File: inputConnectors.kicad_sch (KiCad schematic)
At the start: 2 parts

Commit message: Changes to final schematic
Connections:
- net ESP_USB_DM renamed ESP_USB_D-
- net ESP_USB_DP renamed ESP_USB_D+
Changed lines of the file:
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@@
 		)
 	)
-	(label "ESP_USB_DM"
+	(label "ESP_USB_D-"
 		(at 83.82 59.69 0)
 		(effects
@@
 		)
 	)
-	(label "ESP_USB_DM"
+	(label "ESP_USB_D-"
 		(at 27.94 59.69 0)
 		(effects
@@
 		)
 	)
-	(label "ESP_USB_DP"
+	(label "ESP_USB_D+"
 		(at 27.94 57.15 0)
 		(effects
@@
 		)
 	)
-	(label "ESP_USB_DP"
+	(label "ESP_USB_D+"
 		(at 83.82 57.15 0)
 		(effects
@@
 		)
 	)
-	(global_label "ESP_USB_DP"
+	(global_label "ESP_USB_D+"
 		(shape output)
 		(at 96.52 57.15 0)
@@
 		)
 		(property "Intersheetrefs" "${INTERSHEET_REFS}"
-			(at 108.2513 57.15 0)
+			(at 108.4894 57.15 0)
 			(effects
 				(font
@@
 		)
 	)
-	(global_label "ESP_USB_DM"
+	(global_label "ESP_USB_D-"
 		(shape output)
 		(at 96.52 59.69 0)
@@
 		)
 		(property "Intersheetrefs" "${INTERSHEET_REFS}"
-			(at 108.3942 59.69 0)
+			(at 108.4894 59.69 0)
 			(effects
 				(font

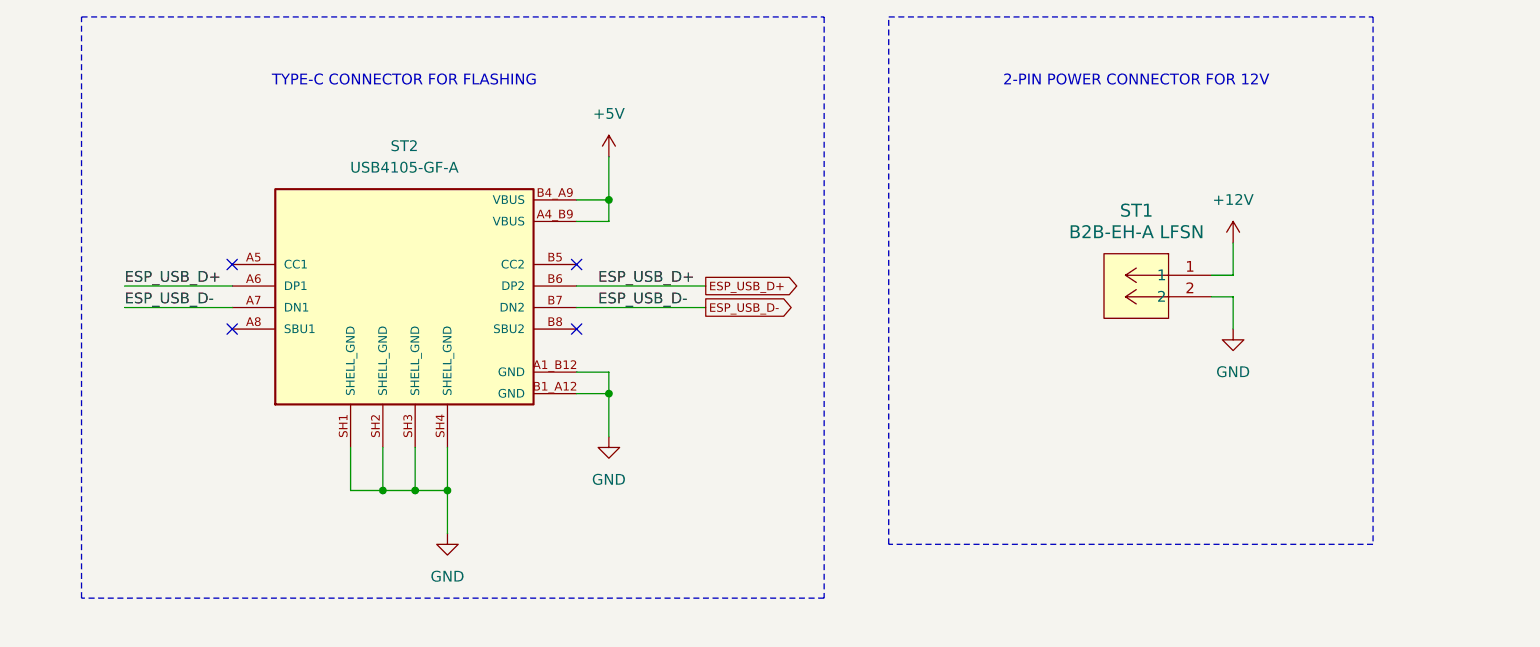
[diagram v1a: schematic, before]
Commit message: Arranged Headers + Added pull-down resistors for type-c conn
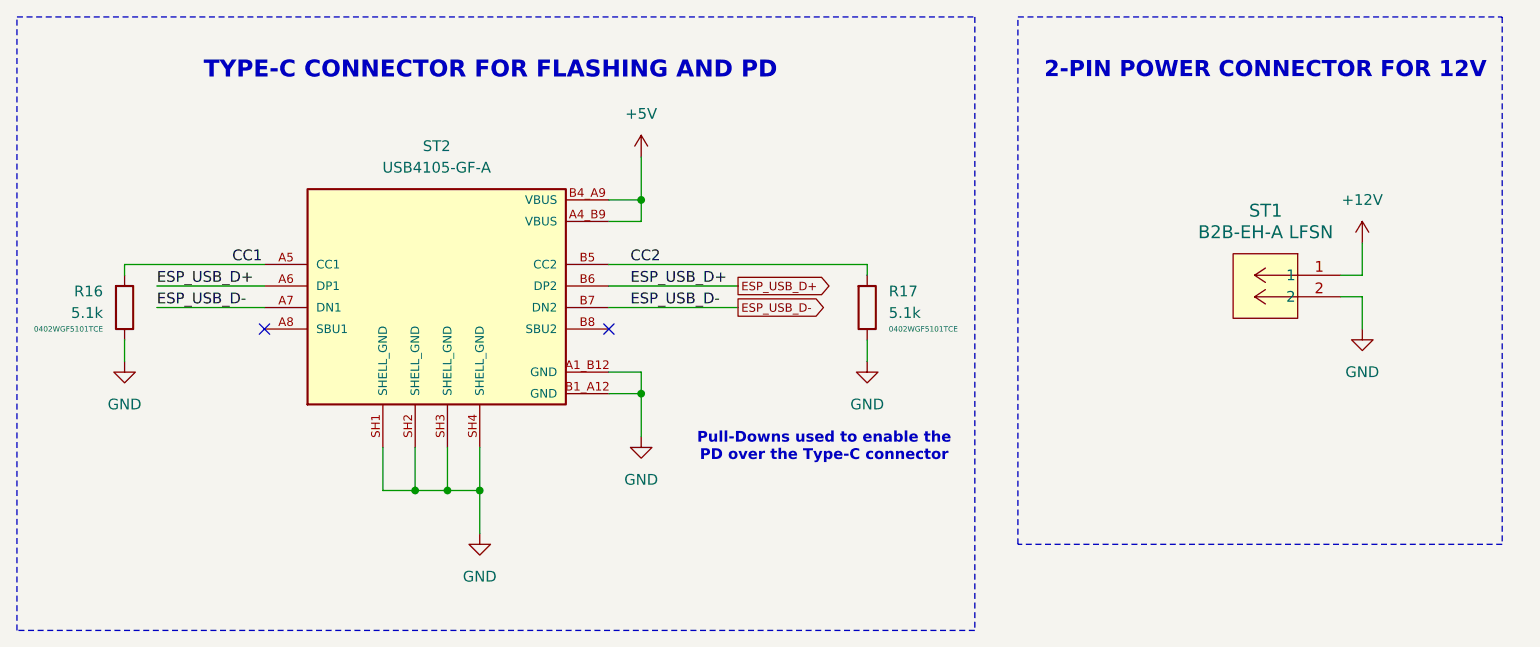
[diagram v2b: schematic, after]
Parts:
- added R16, R17: 5.1k, 0402WGF5101TCE:RESC1005X40N, symbol Project_Resistors:0402WGF5101TCE
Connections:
- net GND: now also R16.2, R17.2
- net CC1: now reaches ST2.A5 (CC1)
- net CC1: now also R16.1
- net CC2: now reaches ST2.B5 (CC2)
- net CC2: now also R17.1
- no-connect marks 4 -> 2
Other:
- note added: "Pull-Downs used to enable the PD over the Type-C connector"
- note added: "TYPE-C CONNECTOR FOR FLASHING AND PD"
- note removed: "TYPE-C CONNECTOR FOR FLASHING"
- moved on the sheet: ST1, ST2

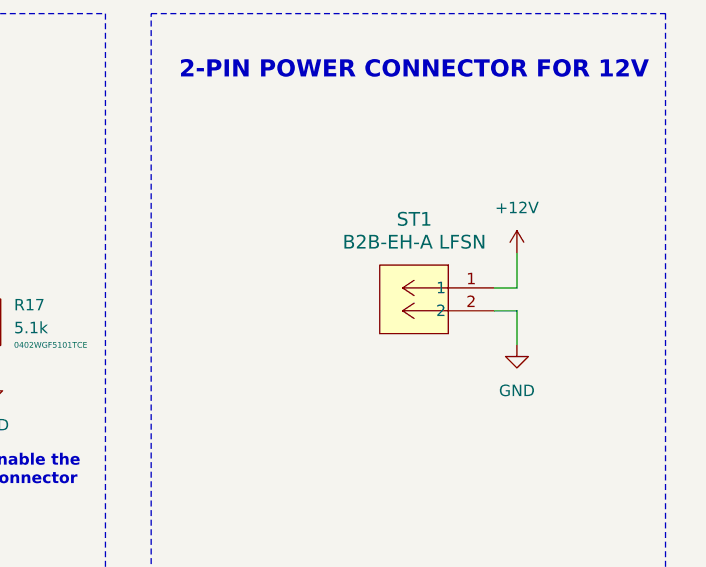
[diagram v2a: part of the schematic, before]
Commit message: JST 2 PIN CONN Changed + Additional 3D Models added
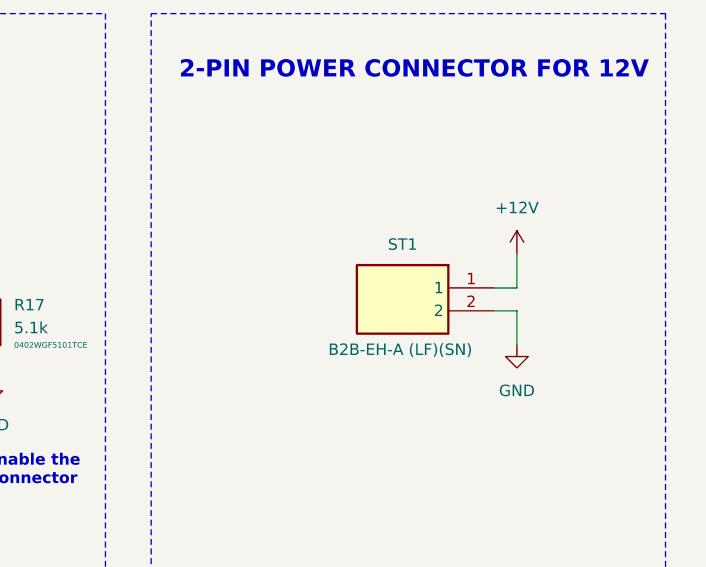
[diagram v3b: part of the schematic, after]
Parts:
- removed ST1: B2B-EH-A LFSN, JST_B2B-EH-A-LF-SN:CONN_B2B-EH-A LFSN_JST, symbol JST_B2B-EH-A-LF-SN:B2B-EH-A_LFSN
- added ST1: B2B-EH-A (LF)(SN), JST_B2B-EH-A(LF)(SN):SHDR2W64P0X250_1X2_750X380X600P, symbol B2B-EH-A(LF)(SN):B2B-EH-A (LF)(SN)
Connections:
- net +12V: now also ST1.1
- net GND: now also ST1.2
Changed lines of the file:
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@@
+	)
+	(symbol
+		(lib_id "B2B-EH-A(LF)(SN):B2B-EH-A (LF)(SN)")
+		(at 171.45 55.88 0)
+		(mirror y)
+		(unit 1)
+		(exclude_from_sim no)
+		(in_bom yes)
+		(on_board yes)
+		(dnp no)
+		(property "Reference" "ST1"
+			(at 161.29 51.054 0)
+			(effects
+				(font
+					(size 1.27 1.27)
+				)
+			)
+		)
+		(property "Value" "B2B-EH-A (LF)(SN)"
+			(at 161.036 62.738 0)
+			(effects
+				(font
+					(size 1.27 1.27)
+				)
+			)
+		)
+		(property "Footprint" "JST_B2B-EH-A(LF)(SN):SHDR2W64P0X250_1X2_750X380X600P"
+			(at 154.94 150.8 0)
+			(effects
+				(font
+					(size 1.27 1.27)
+				)
+				(justify left top)
+				(hide yes)
+			)
+		)
+		(property "Datasheet" "http://www.farnell.com/datasheets/2057210.pdf"
+			(at 154.94 250.8 0)
+			(effects
+				(font
+					(size 1.27 1.27)
+				)
+				(justify left top)
+				(hide yes)
+			)
+		)
+		(property "Description" "JST (JAPAN SOLDERLESS TERMINALS) - B2B-EH-A(LF)(SN) - CONNECTOR, HEADER, 2POS, 2.5MM, 1ROW"
+			(at 171.45 55.88 0)
+			(effects
+				(font
+					(size 1.27 1.27)
+				)
+				(hide yes)
+			)
+		)
+		(property "Height" "6"
+			(at 154.94 450.8 0)
+			(effects
+				(font
+					(size 1.27 1.27)
+				)
+				(justify left top)
+				(hide yes)
+			)
+		)
+		(property "Manufacturer_Name" "JST (JAPAN SOLDERLESS TERMINALS)"
+			(at 154.94 550.8 0)
+			(effects
+				(font
+					(size 1.27 1.27)
+				)
+				(justify left top)
+				(hide yes)
+			)
+		)
+		(property "Manufacturer_Part_Number" "B2B-EH-A(LF)(SN)"
+			(at 154.94 650.8 0)
+			(effects
+				(font
+					(size 1.27 1.27)
+				)
+				(justify left top)
+				(hide yes)
+			)
+		)
+		(property "Mouser Part Number" "N/A"
+			(at 154.94 750.8 0)
+			(effects
+				(font
+					(size 1.27 1.27)
+				)
+				(justify left top)
+				(hide yes)
+			)
+		)
+		(property "Mouser Price/Stock" "https://www.mouser.co.uk/ProductDetail/JST-Commercial/B2B-EH-ALFSN?qs=IKkN%2F947nfCWfpMyWlAobg%3D%3D"
+			(at 154.94 850.8 0)
+			(effects
+				(font
+					(size 1.27 1.27)
+				)
+				(justify left top)
+				(hide yes)
+			)
+		)
+		(property "Arrow Part Number" "B2B-EH-A(LF)(SN)"
+			(at 154.94 950.8 0)
+			(effects
+				(font
+					(size 1.27 1.27)
+				)
+				(justify left top)
+				(hide yes)
+			)
+		)
+		(property "Arrow Price/Stock" "https://www.arrow.com/en/products/b2b-eh-a-lf-sn/jst-manufacturing?region=europe"
+			(at 154.94 1050.8 0)
+			(effects
+				(font
+					(size 1.27 1.27)
+				)
+				(justify left top)
+				(hide yes)
+			)
+		)
+		(pin "2"
+		)
+		(pin "1"
+		)
+		(instances
+			(project ""
+				(path "/fb473f03-1ffd-4345-8dd1-2894c6aef0cc/473821bc-4394-4ccd-b399-e5ac546e238c"
+					(reference "ST1")
+					(unit 1)
+				)
+			)
+		)
 	)
 	(symbol
@@
 					(unit 1)
 				)
-			)
-		)
-	)
-	(symbol
-		(lib_id "JST_B2B-EH-A-LF-SN:B2B-EH-A_LFSN")
-		(at 171.45 55.88 0)
-		(mirror y)
-		(unit 1)
-		(exclude_from_sim no)
-		(in_bom yes)
-		(on_board yes)
-		(dnp no)
-		(fields_autoplaced yes)
-		(property "Reference" "ST1"
-			(at 162.5917 48.26 0)
-			(effects
-				(font
-					(size 1.524 1.524)
-				)
-			)
-		)
-		(property "Value" "B2B-EH-A LFSN"
-			(at 162.5917 50.8 0)
-			(effects
-				(font
-					(size 1.524 1.524)
-				)
-			)
-		)
-		(property "Footprint" "JST_B2B-EH-A-LF-SN:CONN_B2B-EH-A LFSN_JST"
-			(at 171.958 48.768 0)
-			(effects
-				(font
-					(size 1.27 1.27)
-					(italic yes)
-				)
-				(hide yes)
-			)
-		)
-		(property "Datasheet" "B2B-EH-A LFSN"
-			(at 171.704 51.308 0)
-			(effects
-				(font
-					(size 1.27 1.27)
-					(italic yes)
-				)
-				(hide yes)
-			)
-		)
-		(property "Description" ""
-			(at 171.45 55.88 0)
-			(effects
-				(font
-					(size 1.27 1.27)
-				)
-				(hide yes)
-			)
-		)
-		(pin "2"
-		)
-		(pin "1"
-		)
-		(instances
-			(project ""
-				(path "/fb473f03-1ffd-4345-8dd1-2894c6aef0cc/473821bc-4394-4ccd-b399-e5ac546e238c"
-					(reference "ST1")
-					(unit 1)
-				)

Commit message: Промяна по оформление и текст в схемата
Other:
- note added: "5.1 kΩ pull-down resistors on CC lines indicate USB 2.0 peripheral (Device Mode) configuration"
- note removed: "Pull-Downs used to enable the PD over the Type-C connector"
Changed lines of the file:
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@@
 		)
 	)
-	(text "Pull-Downs used to enable the \nPD over the Type-C connector"
+	(text "5.1 kΩ pull-down resistors on CC \nlines indicate USB 2.0 peripheral\n(Device Mode) configuration"
 		(exclude_from_sim no)
-		(at 110.49 76.2 0)
+		(at 110.49 75.946 0)
 		(effects
 			(font
